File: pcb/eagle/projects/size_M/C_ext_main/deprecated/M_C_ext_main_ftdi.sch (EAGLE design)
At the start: 20 parts

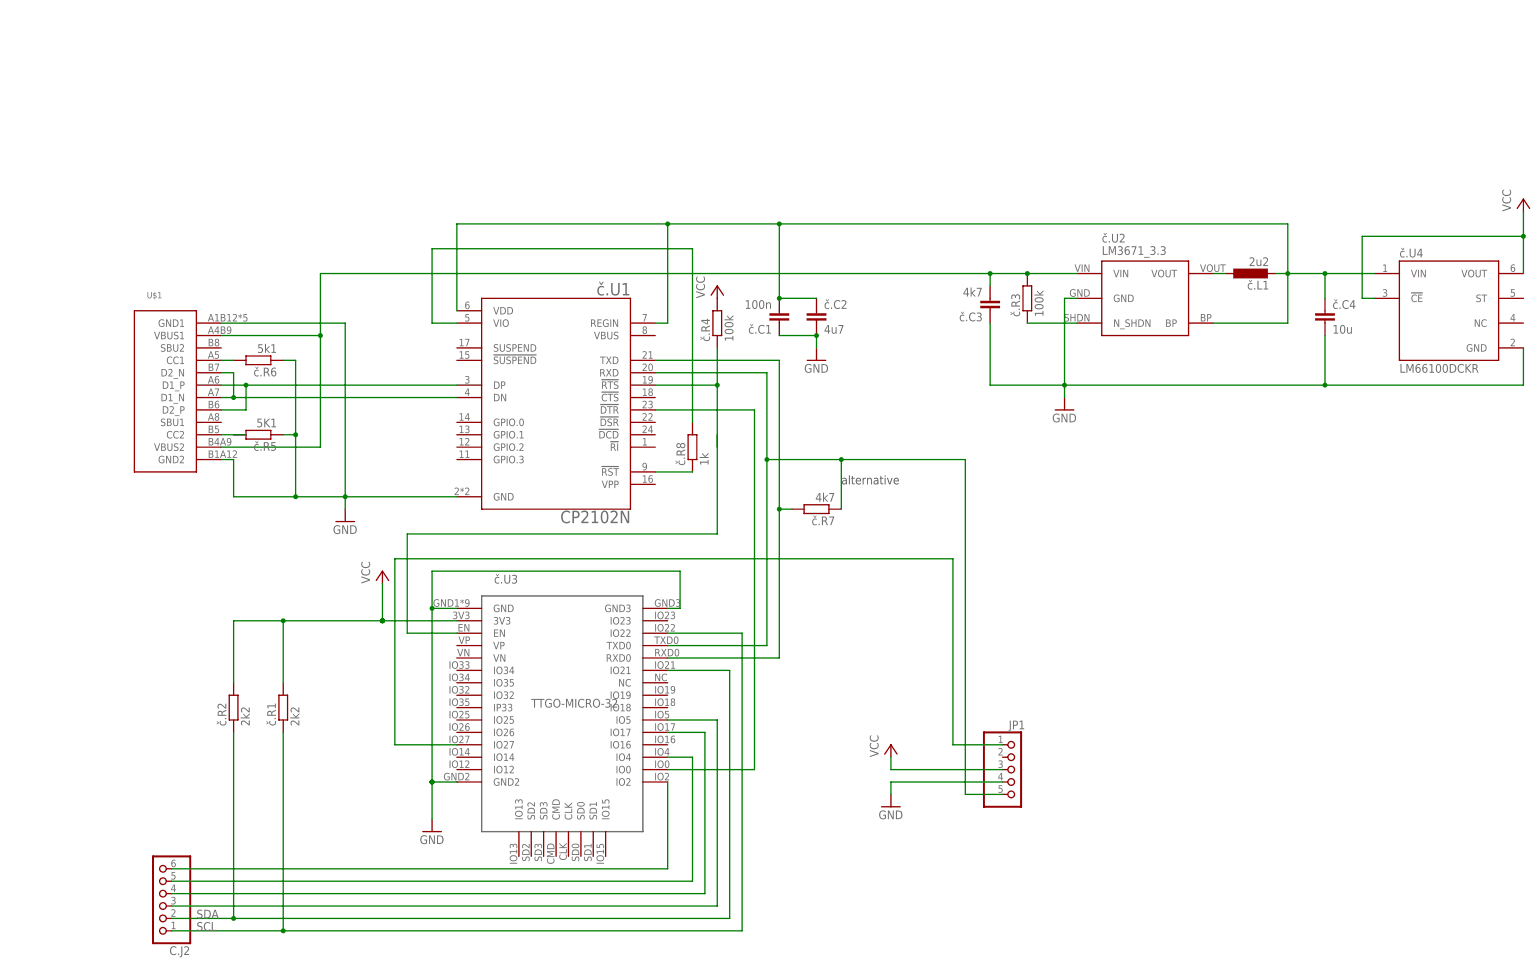
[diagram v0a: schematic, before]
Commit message: version 8 main changes * ideal diode separated 3v3 DC-DC to protect it from back current * smaller package of ina 219 * usage of tssop attiny v2 in adapter * and change of PA5 to PB2 with ^ and ~ (originally used for shield power switch - now PB3) * step motor shield * out signal for BT module
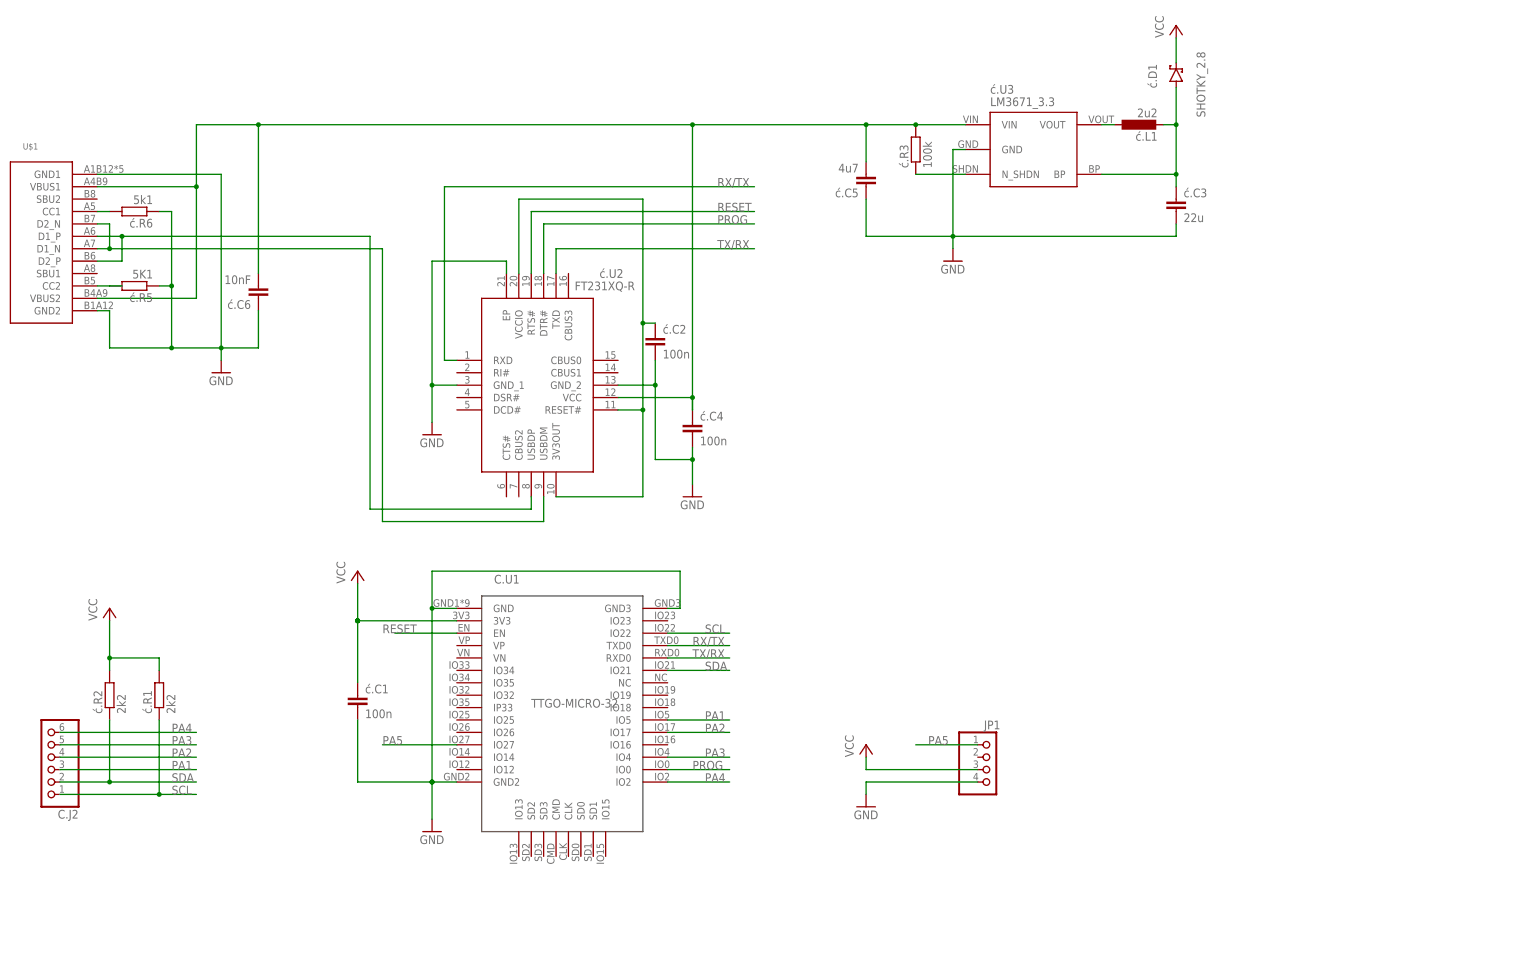
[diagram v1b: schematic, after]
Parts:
- removed č.C1: 100n, rcl:C-EUC0603
- removed č.C2: 4u7, rcl:C-EUC0603
- removed č.C3: 4k7, rcl:C-EUC0603
- removed č.C4: 10u, rcl:C-EUC0603
- removed č.L1: 2u2, rcl:L-EUL3230M
- removed č.R1, č.R2: 2k2, rcl:R-EU_R0603
- removed č.R3, č.R4: 100k, rcl:R-EU_R0603
- removed č.R5: 5K1, rcl:R-EU_R0603
- removed č.R6: 5k1, rcl:R-EU_R0603
- removed č.R7: 4k7, rcl:R-EU_R0603
- removed č.R8: 1k, rcl:R-EU_R0603
- removed č.U1: CP2102N, CP2104:CP2104-F03-GM
- removed č.U2: LM3671_3.3, !stavebnice03:STABILISER_APE8865
- removed č.U4: LM66100DCKR, LM66100DCKR:LM66100DCKR
- added ć.C1, ć.C2, ć.C4: 100n, rcl:C-EUC0603
- added ć.C3: 22u, rcl:C-EUC0805
- added ć.C5: 4u7, rcl:C-EUC0603
- added ć.C6: 10nF, rcl:C-EUC0603
- added ć.D1: SHOTKY_2.8, hugo:SHOTKY_2.8
- added ć.L1: 2u2, rcl:L-EUL3230M
- added ć.R1, ć.R2: 2k2, rcl:R-EU_R0603
- added ć.R3: 100k, rcl:R-EU_R0603
- added ć.R5: 5K1, rcl:R-EU_R0603
- added ć.R6: 5k1, rcl:R-EU_R0603
- added ć.U2: FT231XQ-R, FT231XQ-R:FT231XQ-R
- added ć.U3: LM3671_3.3, !stavebnice03:STABILISER_APE8865
- JP1: device pinhead2:PINHD-1X5 -> pinhead2:PINHD-1X4
- renumbered č.U3 to C.U1
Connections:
- net N$12 renamed PA3
- net N$13 renamed PA2
- net N$14 renamed PA1
- net N$6 renamed PA4
- net N$7 renamed PA5
- removed net N$16: č.R8.1, č.U1.!RST!
- removed net N$8: č.R8.2, č.U1.VIO
- removed net RX: C.U1.TXD0, JP1.5, č.R7.1, č.U1.RXD
- removed net TX: C.U1.RXD0, č.R7.2, č.U1.TXD
- removed net VCC1: č.C1.2, č.C2.1, č.C4.1, č.L1.2, č.U1.REGIN, č.U1.VDD, č.U2.BP, č.U4.VIN
- new net N$15: ć.C2.1, ć.U2.3V3OUT, ć.U2.RESET#, ć.U2.VCCIO
- new net N$5: ć.C3.1, ć.D1.A, ć.L1.2, ć.U3.BP
- new net RX/TX: C.U1.TXD0, ć.U2.RXD
- new net TX/RX: C.U1.RXD0, ć.U2.TXD
- net GND: now also ć.C1.2, ć.C2.2, ć.C3.2, ć.C4.2, ć.C5.1, ć.C6.1, ć.R5.1, ć.R6.1, ć.U2.EP, ć.U2.GND_1, ć.U2.GND_2, ć.U3.GND; no longer č.C1.1, č.C2.2, č.C3.1, č.C4.2, č.R5.1, č.R6.1, č.U1.GND, č.U2.GND, č.U4.GND
- net N$1: now also ć.U2.USBDM; no longer č.U1.DN
- net N$10: now also ć.L1.1, ć.U3.VOUT; no longer č.L1.1, č.U2.VOUT
- net N$11: now also ć.R3.1, ć.U3.N_SHDN; no longer č.R3.1, č.U2.N_SHDN
- net N$2: now also ć.U2.USBDP; no longer č.U1.DP
- net N$3: now also ć.R6.2; no longer č.R6.2
- net N$4: now also ć.R5.2; no longer č.R5.2
- net PROG: now also ć.U2.DTR#; no longer č.U1.!DTR
- net RESET: now also ć.U2.RTS#; no longer č.R4.1, č.U1.!RTS
- net SCL: now also ć.R1.1; no longer č.R1.1
- net SDA: now also ć.R2.1; no longer č.R2.1
- net VCC: now also ć.C1.1, ć.D1.C, ć.R1.2, ć.R2.2; no longer č.R1.2, č.R2.2, č.R4.2, č.U4.!CE, č.U4.VOUT
- net VUSB: now also ć.C4.1, ć.C5.2, ć.C6.2, ć.R3.2, ć.U2.VCC, ć.U3.VIN; no longer č.C3.2, č.R3.2, č.U2.VIN
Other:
- note removed: "alternative"
- moved on the sheet: C.J2, U$1
